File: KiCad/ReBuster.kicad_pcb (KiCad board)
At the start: 4 copper layers, 38 x 38 mm, 40 parts, among them U1 10M02SCU169, U2 LM1117-3.3, U3 SN74CBTD16210, U4 SN74LVC16245ADGVR, U5 SN74CBTD16210, U6 SN74CBTD16210, U7 74LVC2G07GV,125, U8 PLCC_84_plug, U9 PLCC_84_plug

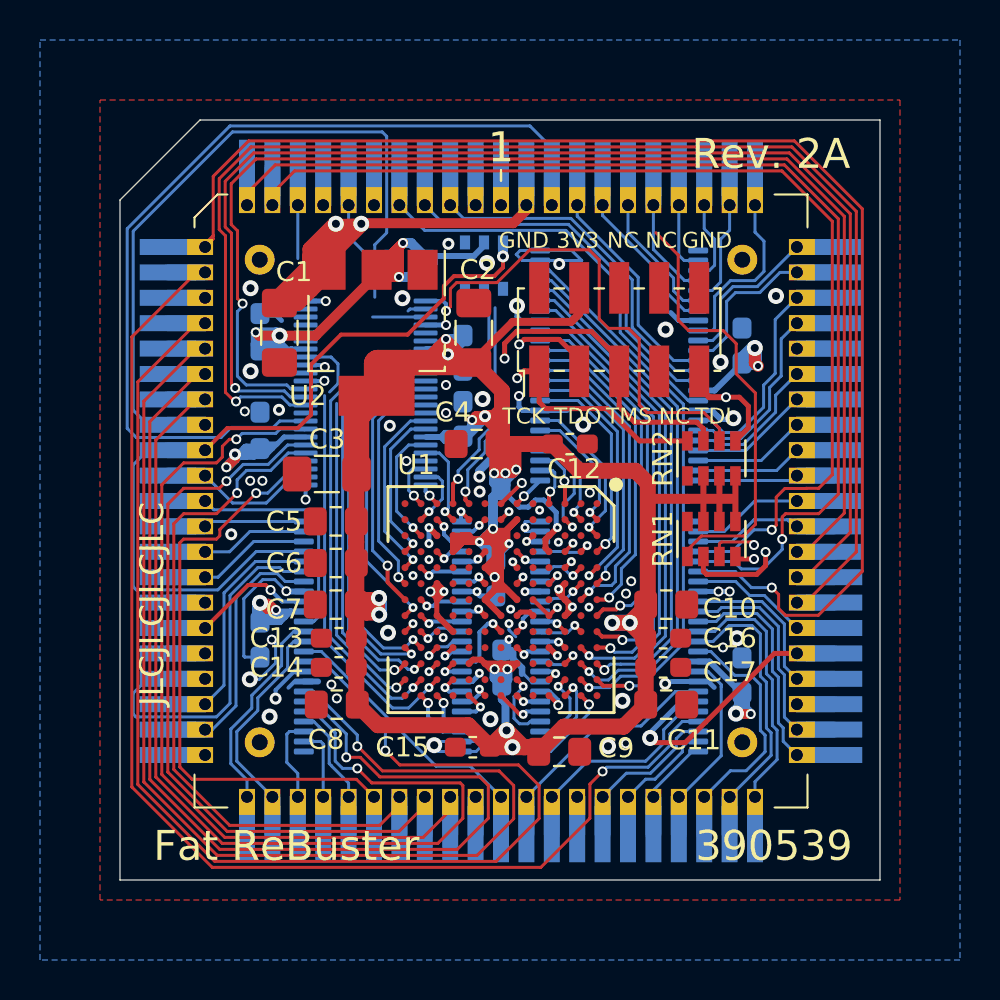
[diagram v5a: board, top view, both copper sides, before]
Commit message: Assign MTACK to pin 23,26 in SN74LVC16245 and M11 in FPGA and route trace
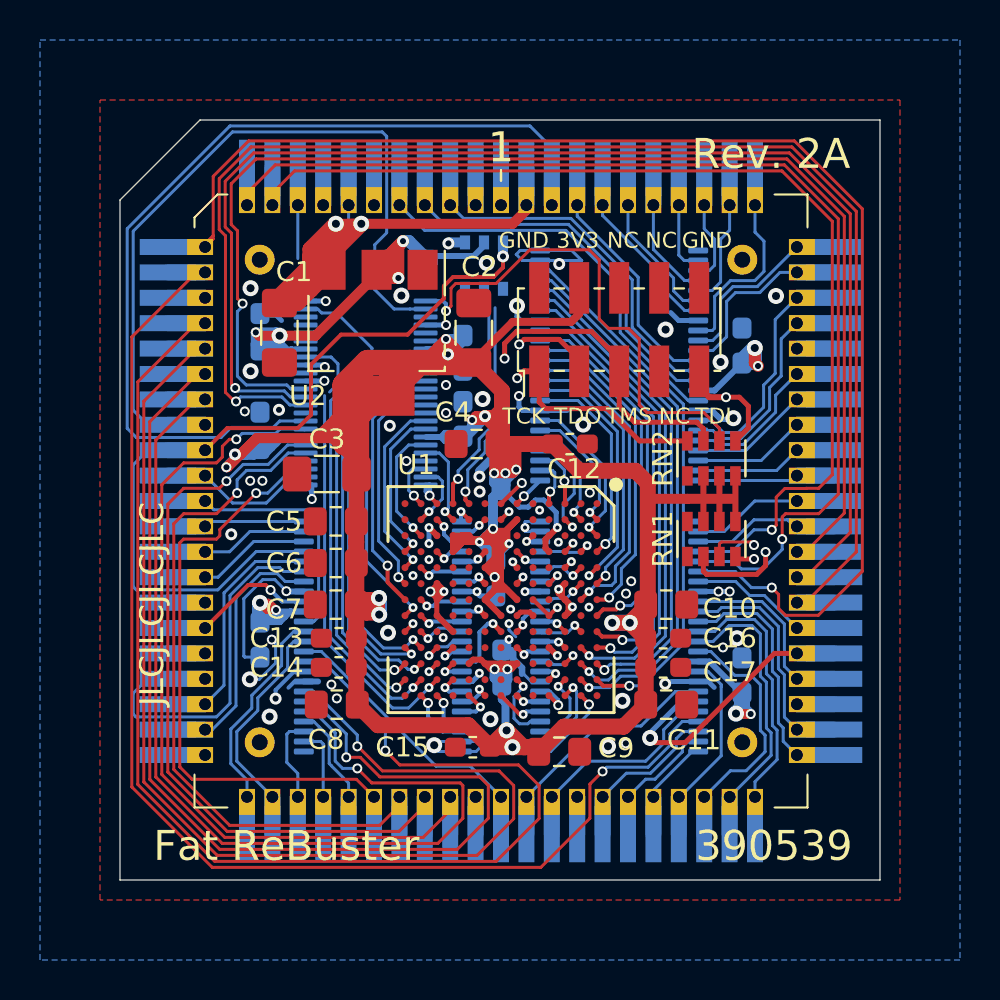
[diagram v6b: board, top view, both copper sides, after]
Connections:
- net Net-(U7-Pad3) renamed MTCR_FPGA
- RN1 pad 1: DIR_U7 -> Net-(RN1-Pad1)
- RN1 pad 8: GND -> Net-(RN1-Pad8)
- U1 pad K1: MTACK_FPGA -> Net-(U1-PadK1)
- U1 pad M11: Net-(U1-PadM11) -> MTACK_FPGA
- U4 pad 23: SIZ1 -> MTACK_FPGA
- U4 pad 26: SIZ1_FPGA -> MTACK
- U7 pad 4: Net-(U7-Pad4) -> MTCR
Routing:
- net DIR_U7: track 29.1 -> 3.15 mm
- net 3V3: track 263.5 -> 288.6 mm
- net Net-(U1-PadM11): track 15.6 -> 0.00 mm, vias 1 -> 0
- net MTACK_FPGA: track 10.9 -> 23.3 mm
- net Net-(U1-PadK1): track 0.00 -> 10.9 mm, vias 0 -> 1
- net FCS: track 5.63 -> 16.0 mm
- net AS_FPGA: track 21.7 -> 19.0 mm
- net MTACK: track 36.0 -> 38.5 mm
- net SIZ0: track 4.81 -> 3.44 mm
- net SIZ1_FPGA: track 20.8 -> 19.8 mm
- net DIR_U4: track 25.7 -> 26.5 mm
- net OE_U4: track 35.8 -> 36.6 mm
- net MTCR: track 52.0 -> 52.5 mm

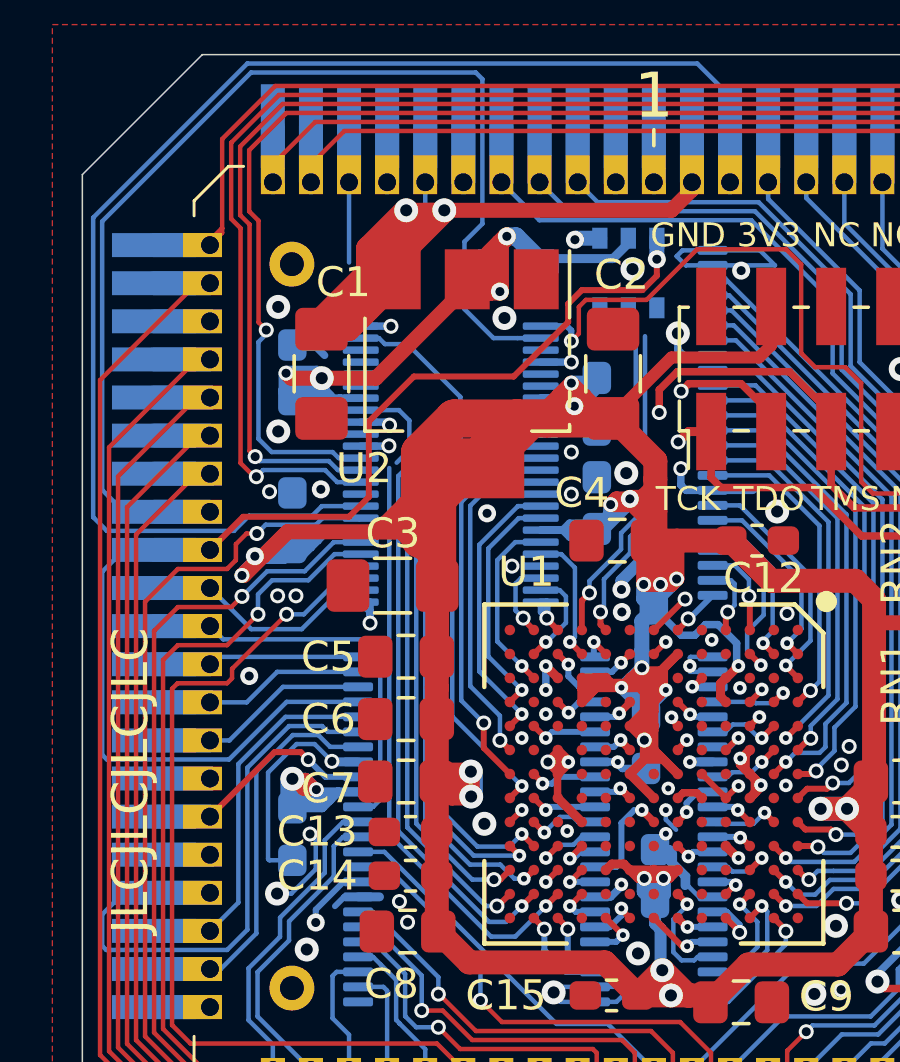
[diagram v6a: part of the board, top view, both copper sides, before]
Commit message: Assign RW to pin 22,27 in SN74LVC16245 and route trace
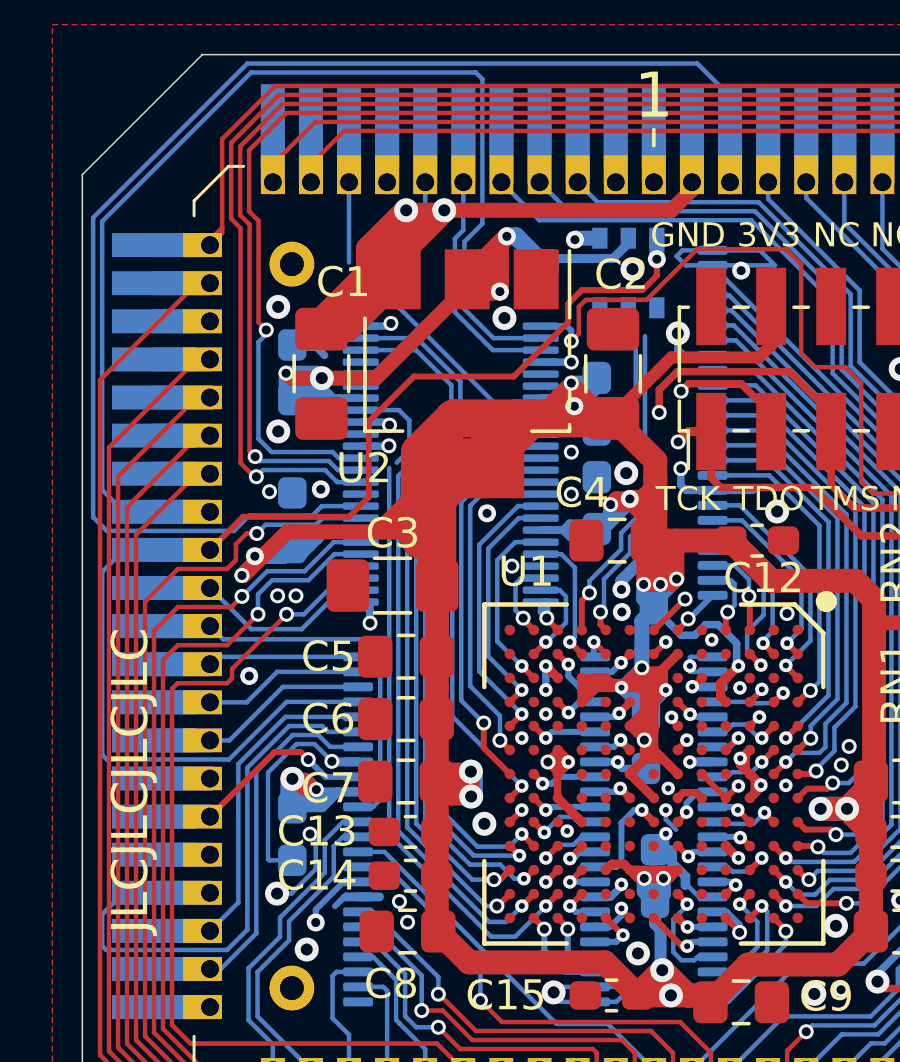
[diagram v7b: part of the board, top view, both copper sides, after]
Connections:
- U4 pad 19: RW -> Net-(U4-Pad19)
- U4 pad 22: AS -> RW_FPGA
- U4 pad 27: AS_FPGA -> RW
- U4 pad 30: RW_FPGA -> Net-(U4-Pad30)
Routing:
- net RW: track 1.87 -> 9.70 mm
- net Net-(U4-Pad32): track 0.00 -> 7.35 mm
- net RW_FPGA: track 15.4 -> 22.6 mm

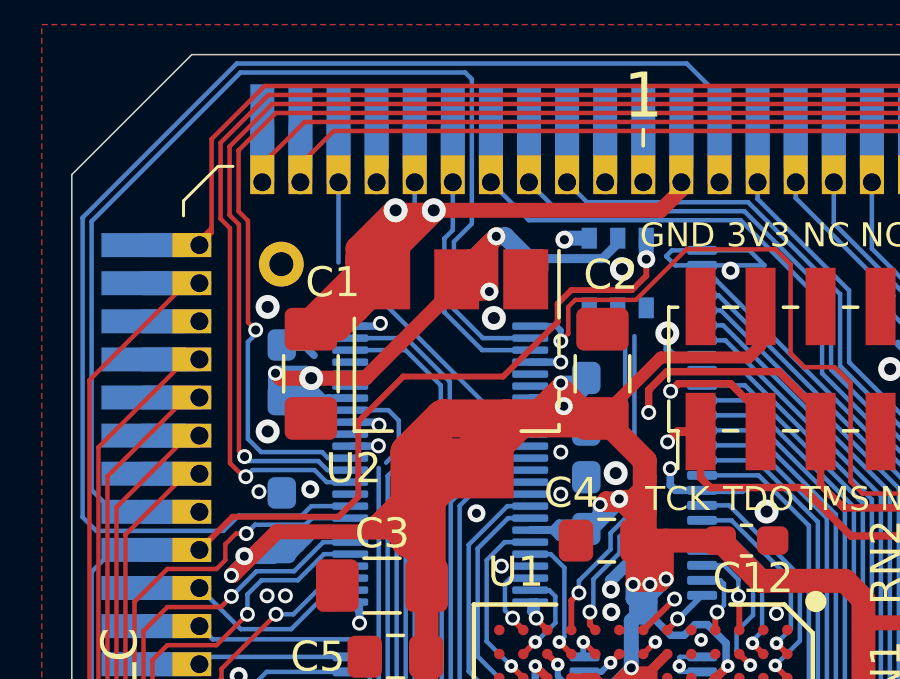
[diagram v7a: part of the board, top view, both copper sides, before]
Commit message: Assign SIZ0 to pin 20,29 in SN74LVC16245 and route trace
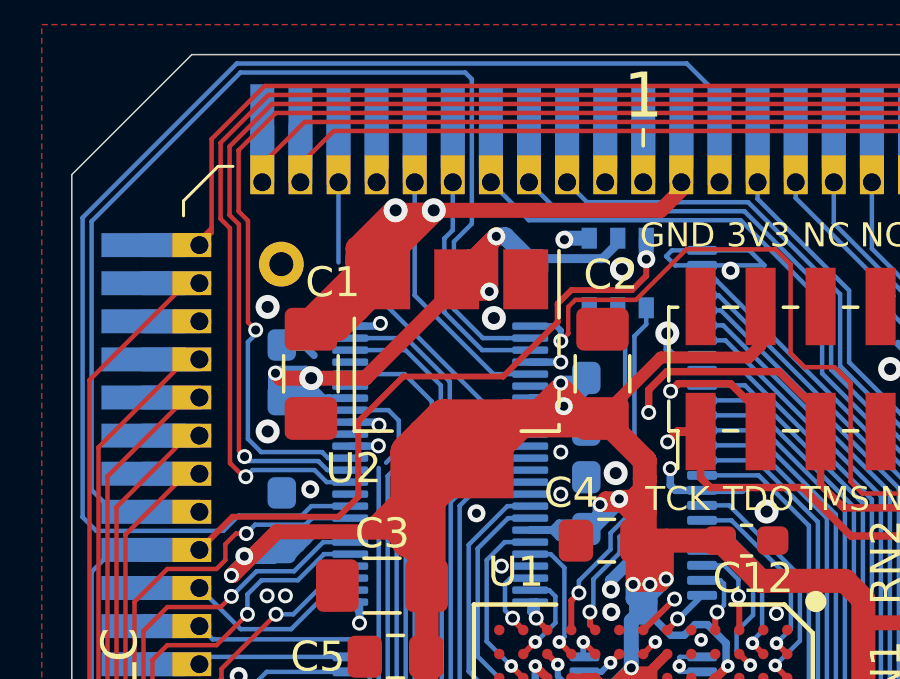
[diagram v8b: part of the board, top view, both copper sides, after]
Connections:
- U4 pad 20: SIZ0 -> SIZ0_FPGA
- U4 pad 29: SIZ0_FPGA -> SIZ0
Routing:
- net 3V3: track 288.6 -> 298.7 mm
- net SIZ0: track 3.44 -> 10.6 mm
- net SIZ0_FPGA: track 16.3 -> 22.5 mm
- net DTACK_FPGA: track 10.9 -> 12.0 mm
- net GND: vias 60 -> 59
